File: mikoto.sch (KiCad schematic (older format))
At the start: 63 parts, among them J1 USB_C_Receptacle_USB2.0, J2 Conn_01x01, J3 Conn_01x01, Q1 DMP21D0UT, Q2 DMP21D0UT, Q3 DMP21D0UT, U1 nRF52840, U2 TP4054, U3 LP5912-3.3DRV, U4 ProMicro_2, Y1 32MHz, Y2 32.768 kHz

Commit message: rename
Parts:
- DUMMY1, DUMMY2: footprint footprints:akami-logo -> footprints:mikoto-logo
- J1: symbol akami:USB_C_Receptacle_USB2.0 -> mikoto:USB_C_Receptacle_USB2.0
- U4: symbol akami:ProMicro_2 -> mikoto:ProMicro_2
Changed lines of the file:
@@
 	9350 5500 9450 5500
 $Comp
-L akami:USB_C_Receptacle_USB2.0 J1
+L mikoto:USB_C_Receptacle_USB2.0 J1
 U 1 1 600E09D4
 P 13700 3850
@@
 	14350 4000 14600 4000
 $Comp
-L akami:ProMicro_2 U4
+L mikoto:ProMicro_2 U4
 U 1 1 6048FFC1
 P 14350 6350
@@
 F 0 "DUMMY1" H 14750 7996 50  0000 L CNN
 F 1 "logo_front" H 14750 7905 50  0000 L CNN
-F 2 "footprints:akami-logo" H 14650 7950 50  0001 C CNN
+F 2 "footprints:mikoto-logo" H 14650 7950 50  0001 C CNN
 F 3 "~" H 14650 7950 50  0001 C CNN
 	1    14650 7950
@@
 F 0 "DUMMY2" H 14750 8196 50  0000 L CNN
 F 1 "logo_back" H 14750 8105 50  0000 L CNN
-F 2 "footprints:akami-logo" H 14650 8150 50  0001 C CNN
+F 2 "footprints:mikoto-logo" H 14650 8150 50  0001 C CNN
 F 3 "~" H 14650 8150 50  0001 C CNN
 	1    14650 8150

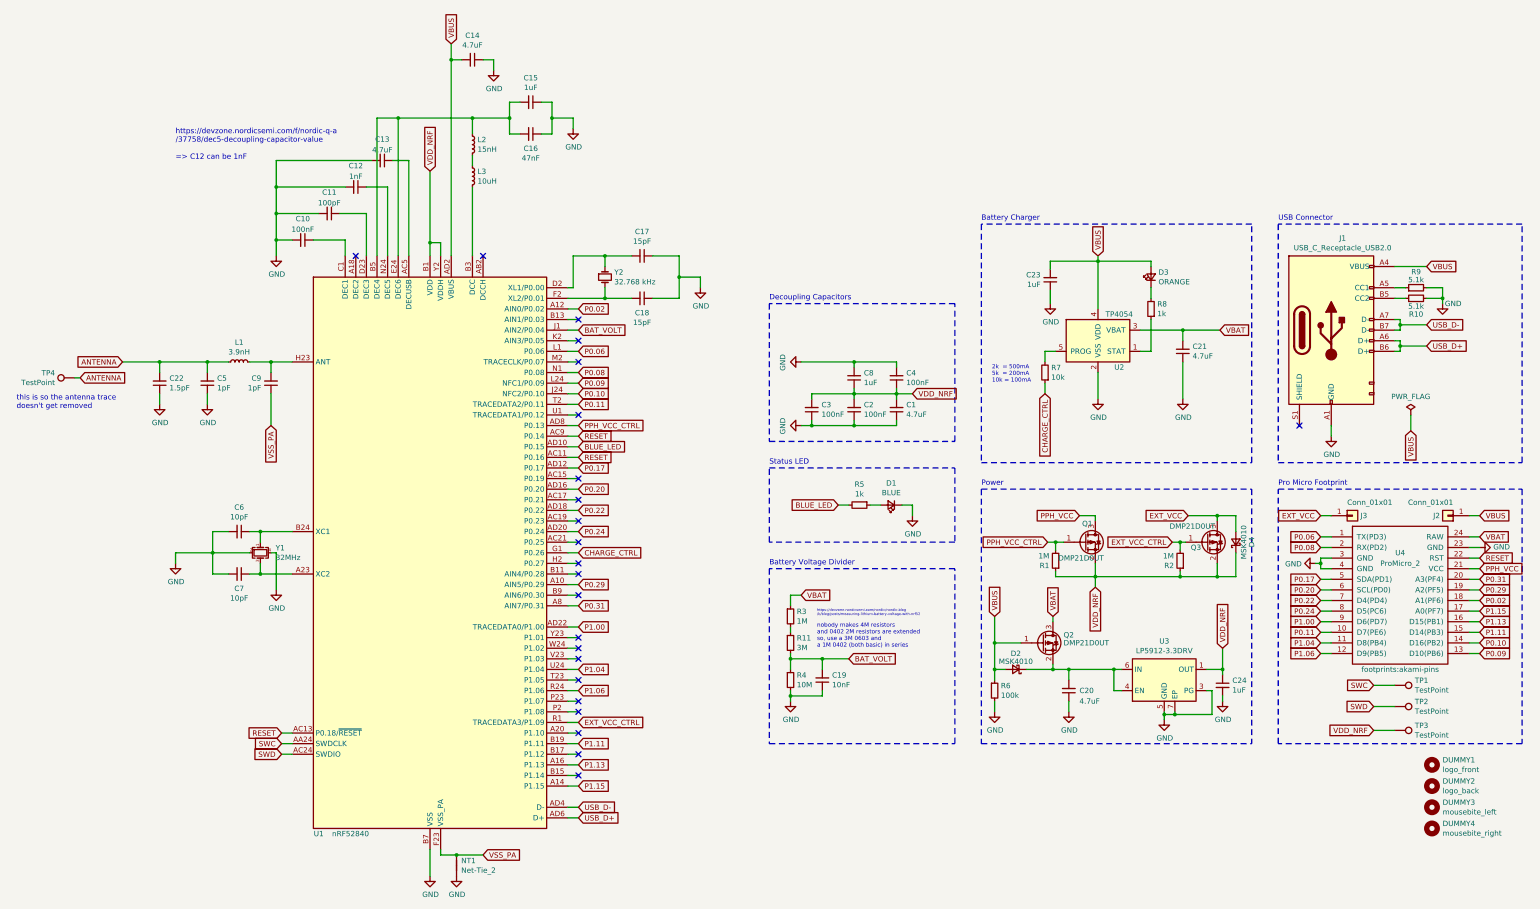
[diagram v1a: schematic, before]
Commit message: rev 4.0
1. Switch to the VDDH (high voltage) power path
2. External power is now 3V3 (PRH) and 4V5 (EXT_5V).
   due to the diode, we are forced to drop ~500mv from VBUS
3. Swap the positions of VBUS and EXT_VCC. This makes us not quite
   compatible with eg. Elite-C, but that was just a bonus anyway.
4. Switch back to the AO3401A mosfet
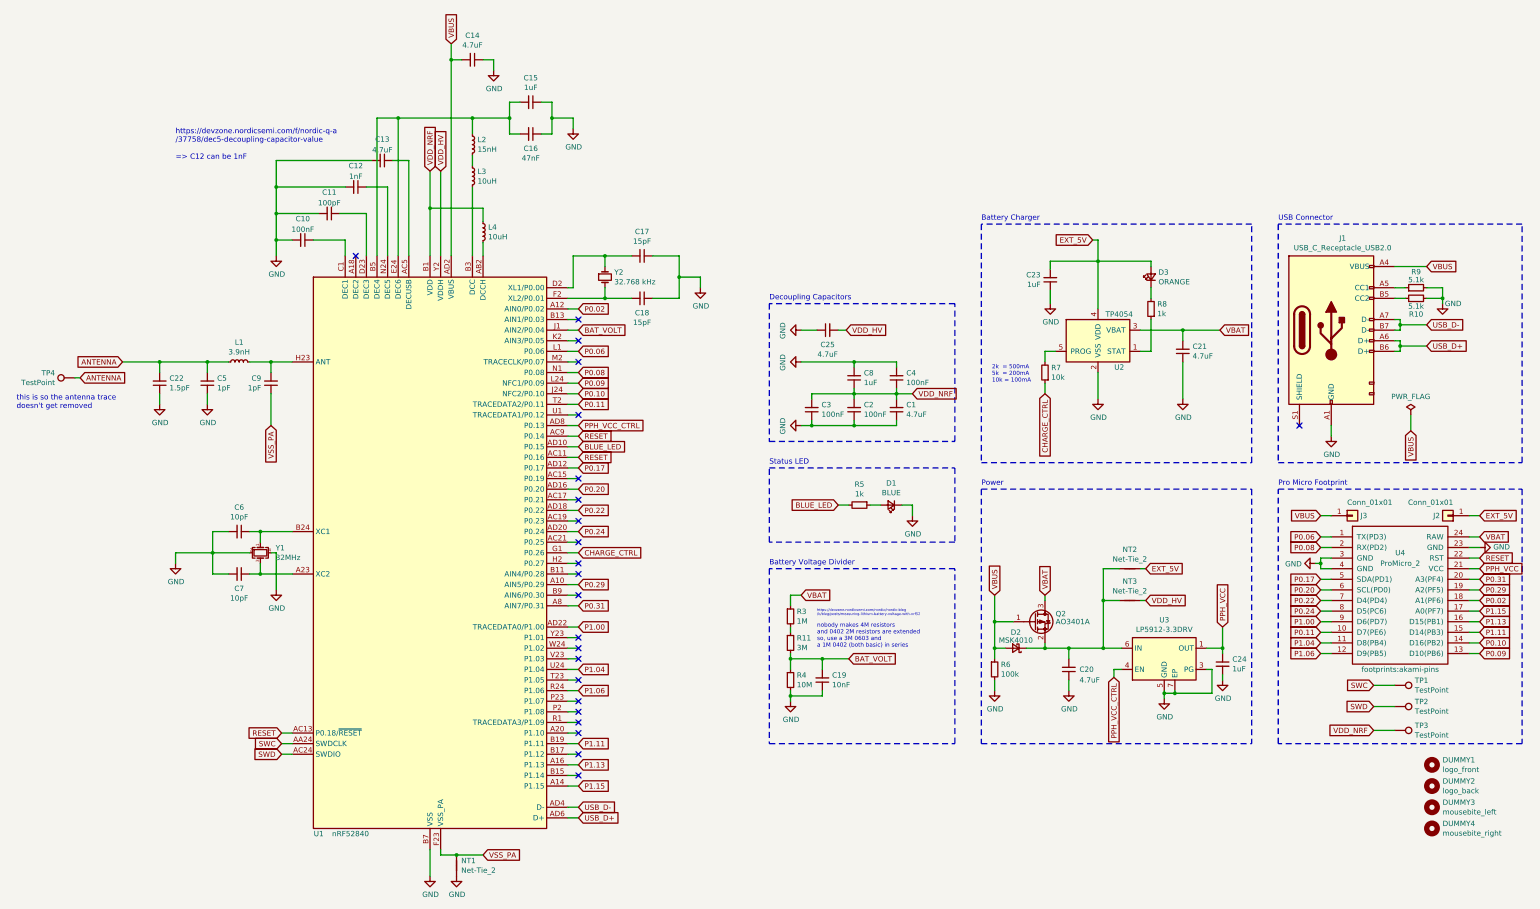
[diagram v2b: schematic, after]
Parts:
- removed D4: MSK4010, Diode_SMD:D_SOD-523, symbol Device:D_Schottky_Small
- removed Q1, Q3: DMP21D0UT, Package_TO_SOT_SMD:SOT-523, symbol Transistor_FET:IRLML9301
- removed R1, R2: 1M, Resistor_SMD:R_0402_1005Metric, symbol Device:R_Small
- added C25: 4.7uF, Capacitor_SMD:C_0603_1608Metric, symbol Device:C_Small
- added L4: 10uH, Inductor_SMD:L_0603_1608Metric, symbol Device:L_Small
- added NT2, NT3: Net-Tie_2, footprints:net-tie-2-0.3mm, symbol Device:Net-Tie_2
- Q2: value DMP21D0UT -> AO3401A; footprint Package_TO_SOT_SMD:SOT-523 -> Package_TO_SOT_SMD:SOT-23
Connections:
- net EXT_VCC is gone; now on net VBUS: J3.1 (Pin_1)
- net GND: now also C25.1
- net PPH_VCC: now also C24.1, U3.1 (OUT)
- net PPH_VCC_CTRL: now also U3.4 (EN)
- net VBUS: no longer C23.2, D3.2 (A), J2.1 (Pin_1), U2.4 (VDD)
- net VDD_NRF: now also L4.1; no longer C24.1, U1.Y2 (VDDH), U3.1 (OUT)
- net at U1.AB2 (DCCH): now also L4.2
- net at C20.2, D2.1 (K), Q2.2 (S)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: now also NT2.2, NT3.2; no longer U3.4 (EN)
- net EXT_VCC_CTRL: no longer names the net of U1.R1 (TRACEDATA3/P1.09)
- new net EXT_5V: C23.2, D3.2 (A), J2.1 (Pin_1), NT2.1, U2.4 (VDD)
- new net VDD_HV: C25.2, NT3.1, U1.Y2 (VDDH)
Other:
- moved on the sheet: C20, C24, D2, Q2, R6, U3

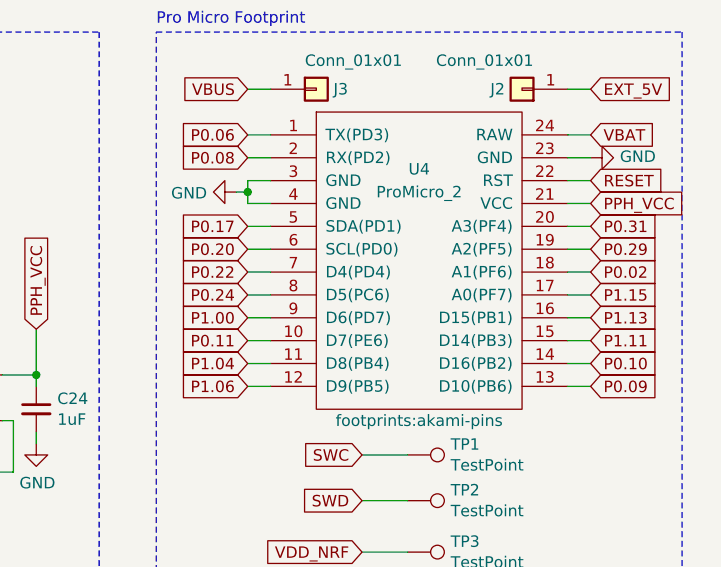
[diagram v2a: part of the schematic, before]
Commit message: rev 4.1
Swap P0.11 and P0.31
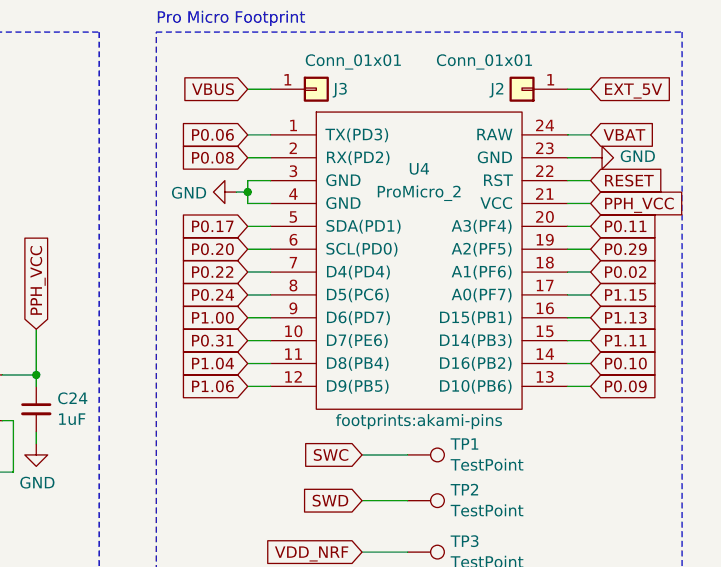
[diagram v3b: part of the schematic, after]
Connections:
- net P0.11: now also U4.20 (A3(PF4)); no longer U4.10 (D7(PE6))
- net P0.31: now also U4.10 (D7(PE6)); no longer U4.20 (A3(PF4))
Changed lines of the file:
@@
 Text GLabel 15100 6300 2    50   Input ~ 0
 P0.29
-Text GLabel 15100 6200 2    50   Input ~ 0
+Text GLabel 13600 6700 0    50   Input ~ 0
 P0.31
 Wire Wire Line
@@
 Text GLabel 13600 6800 0    50   Input ~ 0
 P1.04
-Text GLabel 13600 6700 0    50   Input ~ 0
+Text GLabel 15100 6200 2    50   Input ~ 0
 P0.11
 Wire Wire Line

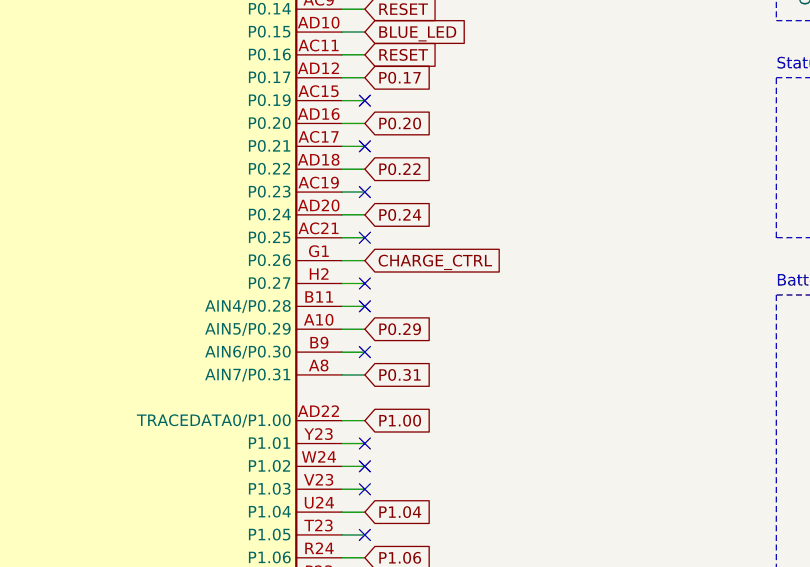
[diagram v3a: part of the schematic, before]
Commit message: rev 4.2
Replace P0.29 with P0.25
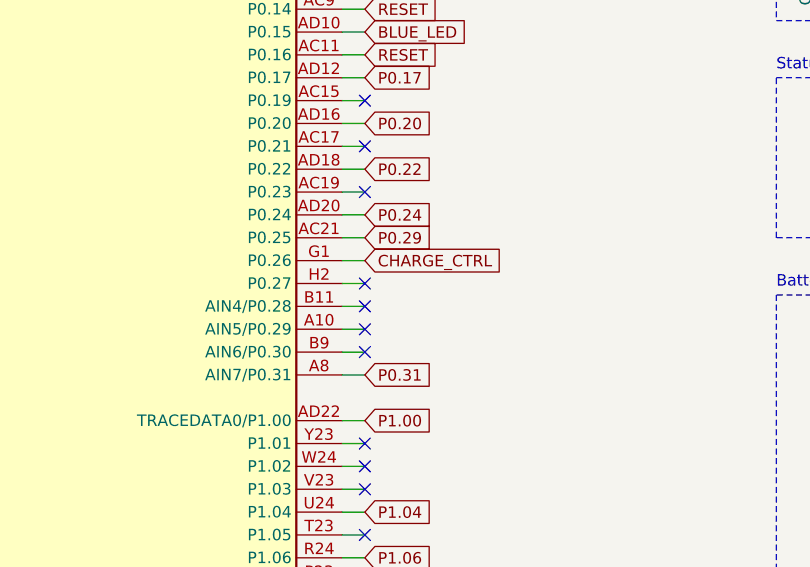
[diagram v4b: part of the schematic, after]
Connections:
- net P0.29: now also U1.AC21 (P0.25); no longer U1.A10 (AIN5/P0.29)
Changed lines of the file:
@@
 Wire Wire Line
 	15000 6400 15100 6400
-Text GLabel 6600 6250 2    50   Input ~ 0
+Text GLabel 6600 5850 2    50   Input ~ 0
 P0.29
 Text GLabel 6600 6450 2    50   Input ~ 0
@@
 NoConn ~ 6600 5450
 NoConn ~ 6600 5650
-NoConn ~ 6600 5850
 Wire Wire Line
 	13700 6400 13600 6400
@@
 	-1   0    0    1
 $EndComp
+NoConn ~ 6600 6250
 $EndSCHEMATC

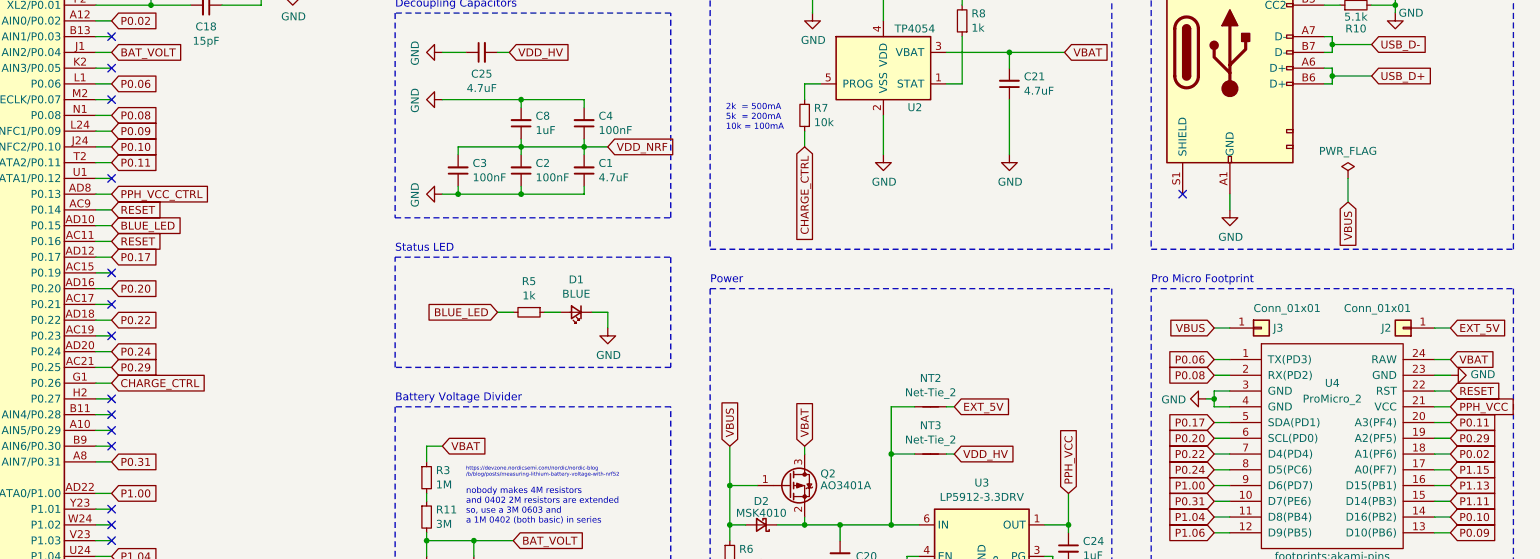
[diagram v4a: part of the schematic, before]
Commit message: rev 4.3
1. (re)-swap VBUS and EXT_5V, so we are back to the original layout
2. change the power plane copper fill to be VBUS for the top half
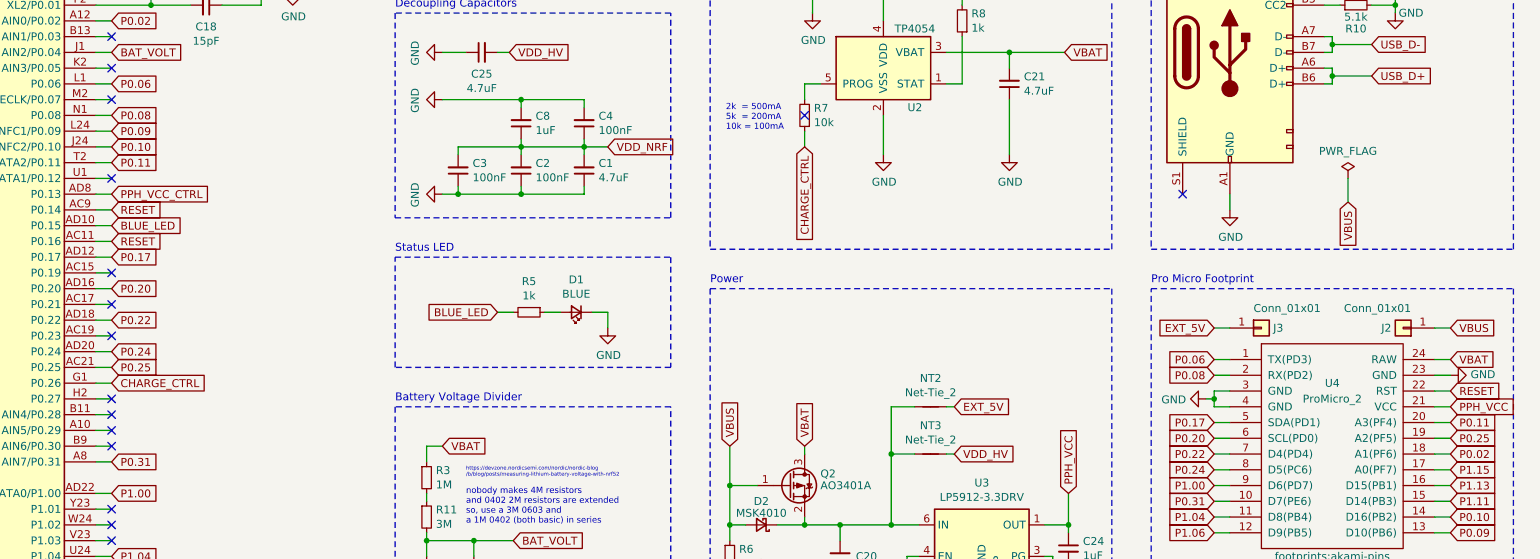
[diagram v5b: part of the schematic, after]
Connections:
- net EXT_5V: now also J3.1 (Pin_1); no longer J2.1 (Pin_1)
- net VBUS: now also J2.1 (Pin_1); no longer J3.1 (Pin_1)
- net P0.29 renamed P0.25
- no-connect marks 23 -> 24
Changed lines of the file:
@@
 	15000 6400 15100 6400
 Text GLabel 6600 5850 2    50   Input ~ 0
-P0.29
+P0.25
 Text GLabel 6600 6450 2    50   Input ~ 0
 P0.31
 Text GLabel 15100 6300 2    50   Input ~ 0
-P0.29
+P0.25
 Text GLabel 13600 6700 0    50   Input ~ 0
 P0.31
@@
 	12950 5350 12950 7750
 Text GLabel 13600 5600 0    50   Input ~ 0
-VBUS
-Text GLabel 15100 5600 2    50   Input ~ 0
 EXT_5V
 Text GLabel 10525 6350 1    50   Input ~ 0
@@
 $EndComp
 NoConn ~ 6600 6250
+Text GLabel 15100 5600 2    50   Input ~ 0
+VBUS
+NoConn ~ 11000 4250
 $EndSCHEMATC

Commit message: rev 4.7
1. replace exotic LP5912 LDO with more common AP2112K
2. replace AO3401A mosfet with DMP2165UW (smaller package)
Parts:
- removed U3: LP5912-3.3DRV, Package_SON:WSON-6-1EP_2x2mm_P0.65mm_EP1x1.6mm_ThermalVias, symbol Regulator_Linear:LP5912-3.3DRV
- added U3: AP2112K-3.3, Package_TO_SOT_SMD:SOT-23-5, symbol Regulator_Linear:AP2112K-3.3
- Q2: value AO3401A -> DMP2165UW; footprint Package_TO_SOT_SMD:SOT-23 -> Package_TO_SOT_SMD:SOT-323_SC-70; symbol Transistor_FET:IRLML9301 -> Device:Q_PMOS_GSD; LCSC Part C150733 -> C388477
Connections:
- net GND: now also U3.2 (GND)
- net PPH_VCC: now also U3.5 (VOUT)
- net PPH_VCC_CTRL: now also U3.3 (EN)
- net at C20.2, D2.1 (K), NT2.2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: now also U3.1 (VIN)
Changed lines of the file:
@@
 	10525 6850 10525 6950
 $Comp
-L Transistor_FET:IRLML9301 Q2
+L Device:Q_PMOS_GSD Q2
 U 1 1 60065EE0
 P 10900 6600
 F 0 "Q2" H 11100 6675 50  0000 L CNN
-F 1 "AO3401A" H 11100 6600 50  0000 L CNN
-F 2 "Package_TO_SOT_SMD:SOT-23" H 11100 6525 50  0001 L CIN
+F 1 "DMP2165UW" H 11100 6600 50  0000 L CNN
+F 2 "Package_TO_SOT_SMD:SOT-323_SC-70" H 11100 6525 50  0001 L CIN
 F 3 "" H 10900 6600 50  0001 L CNN
-F 4 "C150733" H 10900 6600 50  0001 C CNN "LCSC Part"
+F 4 "C388477" H 10900 6600 50  0001 C CNN "LCSC Part"
 	1    10900 6600
 	1    0    0    -1
@@
 	-1   0    0    1
 $EndComp
-$Comp
-L Regulator_Linear:LP5912-3.3DRV U3
-U 1 1 60D2A9A8
-P 12125 6950
-F 0 "U3" H 12125 7317 50  0000 C CNN
-F 1 "LP5912-3.3DRV" H 12125 7226 50  0000 C CNN
-F 2 "Package_SON:WSON-6-1EP_2x2mm_P0.65mm_EP1x1.6mm_ThermalVias" H 12125 7300 50  0001 C CNN
-F 3 "http://www.ti.com/lit/ds/symlink/lp5912.pdf" H 12125 7450 50  0001 C CNN
-F 4 "C134121" H 12125 6950 50  0001 C CNN "LCSC Part"
-	1    12125 6950
-	1    0    0    -1
-$EndComp
-Wire Wire Line
-	11650 7050 11725 7050
-Wire Wire Line
-	12525 6850 12675 6850
-Wire Wire Line
-	12525 7050 12575 7050
 Wire Wire Line
 	11225 6850 11225 6950
 Connection ~ 11225 6850
-Wire Wire Line
-	12225 7250 12225 7275
 Wire Wire Line
 	11225 7250 11225 7150
@@
 Wire Wire Line
 	11000 6350 11000 6400
-Wire Wire Line
-	12125 7250 12125 7275
-Wire Wire Line
-	12125 7275 12225 7275
-Connection ~ 12225 7275
-Wire Wire Line
-	12225 7275 12575 7275
-Wire Wire Line
-	12575 7050 12575 7275
-Wire Wire Line
-	12125 7325 12125 7275
-Connection ~ 12125 7275
-Text GLabel 11650 7125 3    50   Input ~ 0
+Text GLabel 11700 7050 3    50   Input ~ 0
 PPH_VCC_CTRL
 Wire Wire Line
@@
 Wire Wire Line
 	9050 3850 9125 3850
-Wire Wire Line
-	11650 7125 11650 7050
 Text GLabel 11950 6400 2    50   Input ~ 0
 VDD_HV
@@
 	11550 6850 11550 6400
 Connection ~ 11550 6850
-Wire Wire Line
-	11550 6850 11725 6850
 Connection ~ 11550 6400
 NoConn ~ 6600 7550
@@
 VBUS
 NoConn ~ 11000 4250
+$Comp
+L Regulator_Linear:AP2112K-3.3 U3
+U 1 1 6128CF57
+P 12125 6950
+F 0 "U3" H 12125 7292 50  0000 C CNN
+F 1 "AP2112K-3.3" H 12125 7201 50  0000 C CNN
+F 2 "Package_TO_SOT_SMD:SOT-23-5" H 12125 7275 50  0001 C CNN
+F 3 "https://www.diodes.com/assets/Datasheets/AP2112.pdf" H 12125 7050 50  0001 C CNN
+F 4 "C51118" H 12125 6950 50  0001 C CNN "LCSC Part"
+	1    12125 6950
+	1    0    0    -1
+$EndComp
+Wire Wire Line
+	12125 7250 12125 7325
+Wire Wire Line
+	11700 7050 11700 6950
+Wire Wire Line
+	11700 6950 11825 6950
+Wire Wire Line
+	11550 6850 11825 6850
+Wire Wire Line
+	12425 6850 12675 6850
 $EndSCHEMATC
